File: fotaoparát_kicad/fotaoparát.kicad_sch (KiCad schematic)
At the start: 5 parts, among them IC1 W25Q256JVEIQ, J2 Micro_SD_Card_Det1, U2 CR2013-MI2120

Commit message: blablabla
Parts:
- removed U2: CR2013-MI2120, Display:CR2013-MI2120, symbol Driver_Display:CR2013-MI2120
- added U2: ~, symbol st_lib:ST7796s
- J2: footprint (none) -> Connector_Card:microSD_HC_Hirose_DM3D-SF
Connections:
- net +3.3V: now also R1.1, U2.1 (VCC), U2.7 (RD); no longer R1.2
- net GND: now also U2.2 (GND)
- net at U1.57 (GPIO28): now also U2.23 (D15)
- net at U1.58 (GPIO29): now also U2.22 (D14)
- net at U1.60 (GPIO30): now also U2.21 (D13)
- net at U1.61 (GPIO31): now also U2.19 (D11)
- net at U1.63 (GPIO32): now also U2.18 (D10)
- net at U1.64 (GPIO33): now also U2.17 (D9)
- net at U1.65 (GPIO34): now also U2.16 (D8)
- net at U1.66 (GPIO35): now also U2.15 (D7)
- net at U1.67 (VDD_PSRAM_1): now also U2.14 (D6)
- net at U1.68 (GPIO36): now also U2.13 (D5)
- net at U1.69 (GPIO37): now also U2.12 (D4)
- net at U1.70 (GPIO38): now also U2.11 (D3)
- net at U1.80 (GPIO39): now also U2.10 (D2)
- net at U1.81 (GPIO40): now also U2.9 (D1)
- net at U1.82 (GPIO41): now also U2.8 (D0)
- net at U1.83 (GPIO42): now also U2.6 (WR)
- net at U1.84 (GPIO43): now also U2.5 (RS/DC)
- net at U1.86 (GPIO44): now also U2.4 (CS)
- net at U1.87 (GPIO45): now also U2.3 (RESET)
- net at IC1.3 (DO_(IO1)_2), IC1.7 (IO3): now also R1.2; no longer R1.1
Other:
- moved on the sheet: IC1, J2, R1, U1

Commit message: nevim, neco tu vadi
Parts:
- U2: footprint (none) -> stlib:ST7796s_40PIN_0.8MM
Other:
- moved on the sheet: IC1, J2, R1, U1, U2

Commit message: Mirne nakresove zmeny
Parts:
- added J1: Conn_01x22, Connector_FFC-FPC:Amphenol_F32Q-1A7x1-11022_1x22-1MP_P0.5mm_Horizontal, symbol Connector_Generic:Conn_01x22
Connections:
- net +3.3V: now also J1.1 (Pin_1), J1.2 (Pin_2); no longer U1.85 (VDD_IO_5)
- net GND: now also J1.13 (Pin_13), J1.16 (Pin_16), J1.19 (Pin_19), J1.22 (Pin_22)
- net at U1.42 (CSI_DATAN0): now also J1.21 (Pin_21)
- net at U1.43 (CSI_DATAP0): now also J1.20 (Pin_20)
- net at U1.44 (CSI_CLKP): now also J1.14 (Pin_14)
- net at U1.45 (CSI_CLKN): now also J1.15 (Pin_15)
- net at U1.46 (CSI_DATAN1): now also J1.18 (Pin_18)
- net at U1.47 (CSI_DATAP1): now also J1.17 (Pin_17)
- net at U1.57 (GPIO28): now also J1.3 (Pin_3); no longer U2.23 (D15)
- net at U1.58 (GPIO29): now also J1.4 (Pin_4); no longer U2.22 (D14)
- net at U1.60 (GPIO30): now also J1.6 (Pin_6); no longer U2.21 (D13)
- net at U1.61 (GPIO31): no longer U2.19 (D11)
- net at U1.63 (GPIO32): no longer U2.18 (D10)
- net at U1.64 (GPIO33): no longer U2.17 (D9)
- net at U1.65 (GPIO34): no longer U2.16 (D8)
- net at U1.66 (GPIO35): no longer U2.15 (D7)
- net at U1.67 (VDD_PSRAM_1): no longer U2.14 (D6)
- net at U1.68 (GPIO36): no longer U2.13 (D5)
- net at U1.69 (GPIO37): no longer U2.12 (D4)
- net at U1.70 (GPIO38): no longer U2.11 (D3)
- net at U1.80 (GPIO39): no longer U2.10 (D2)
- net at U1.81 (GPIO40): no longer U2.9 (D1)
- net at U1.82 (GPIO41): no longer U2.8 (D0)
- net at U1.83 (GPIO42): no longer U2.6 (WR)
- net at U1.84 (GPIO43): no longer U2.5 (RS/DC)
- net at U1.86 (GPIO44): no longer U2.4 (CS)
- net at U1.87 (GPIO45): no longer U2.3 (RESET)
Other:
- moved on the sheet: IC1, J2, R1, U1, U2

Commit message: PCB routing 22pin na kameru
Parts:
- J1: footprint Connector_FFC-FPC:Amphenol_F32Q-1A7x1-11022_1x22-1MP_P0.5mm_Horizontal -> rnd_shit_co_nema_symboly:Hirose_FH12-22S-0.5SH
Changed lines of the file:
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@@
 			)
 		)
-		(property "Footprint" "Connector_FFC-FPC:Amphenol_F32Q-1A7x1-11022_1x22-1MP_P0.5mm_Horizontal"
+		(property "Footprint" "rnd_shit_co_nema_symboly:Hirose_FH12-22S-0.5SH"
 			(at 312.42 185.42 0)
 			(effects

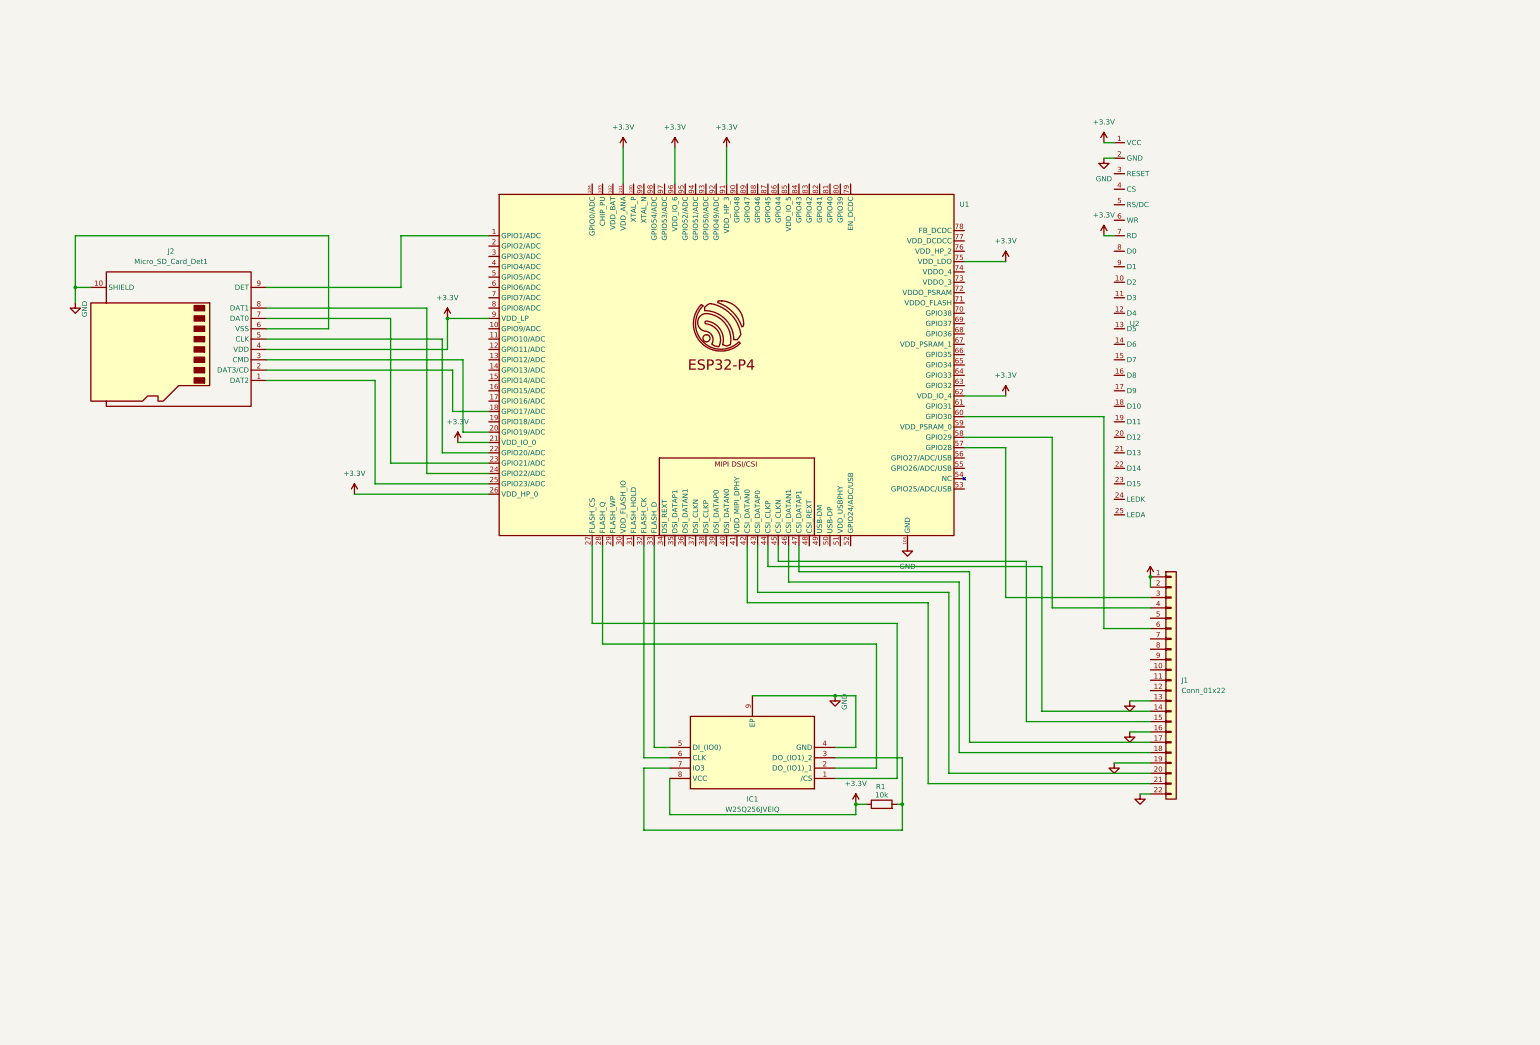
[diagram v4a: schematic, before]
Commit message: Uprava pcb, finalni predelani (snad)  kamery
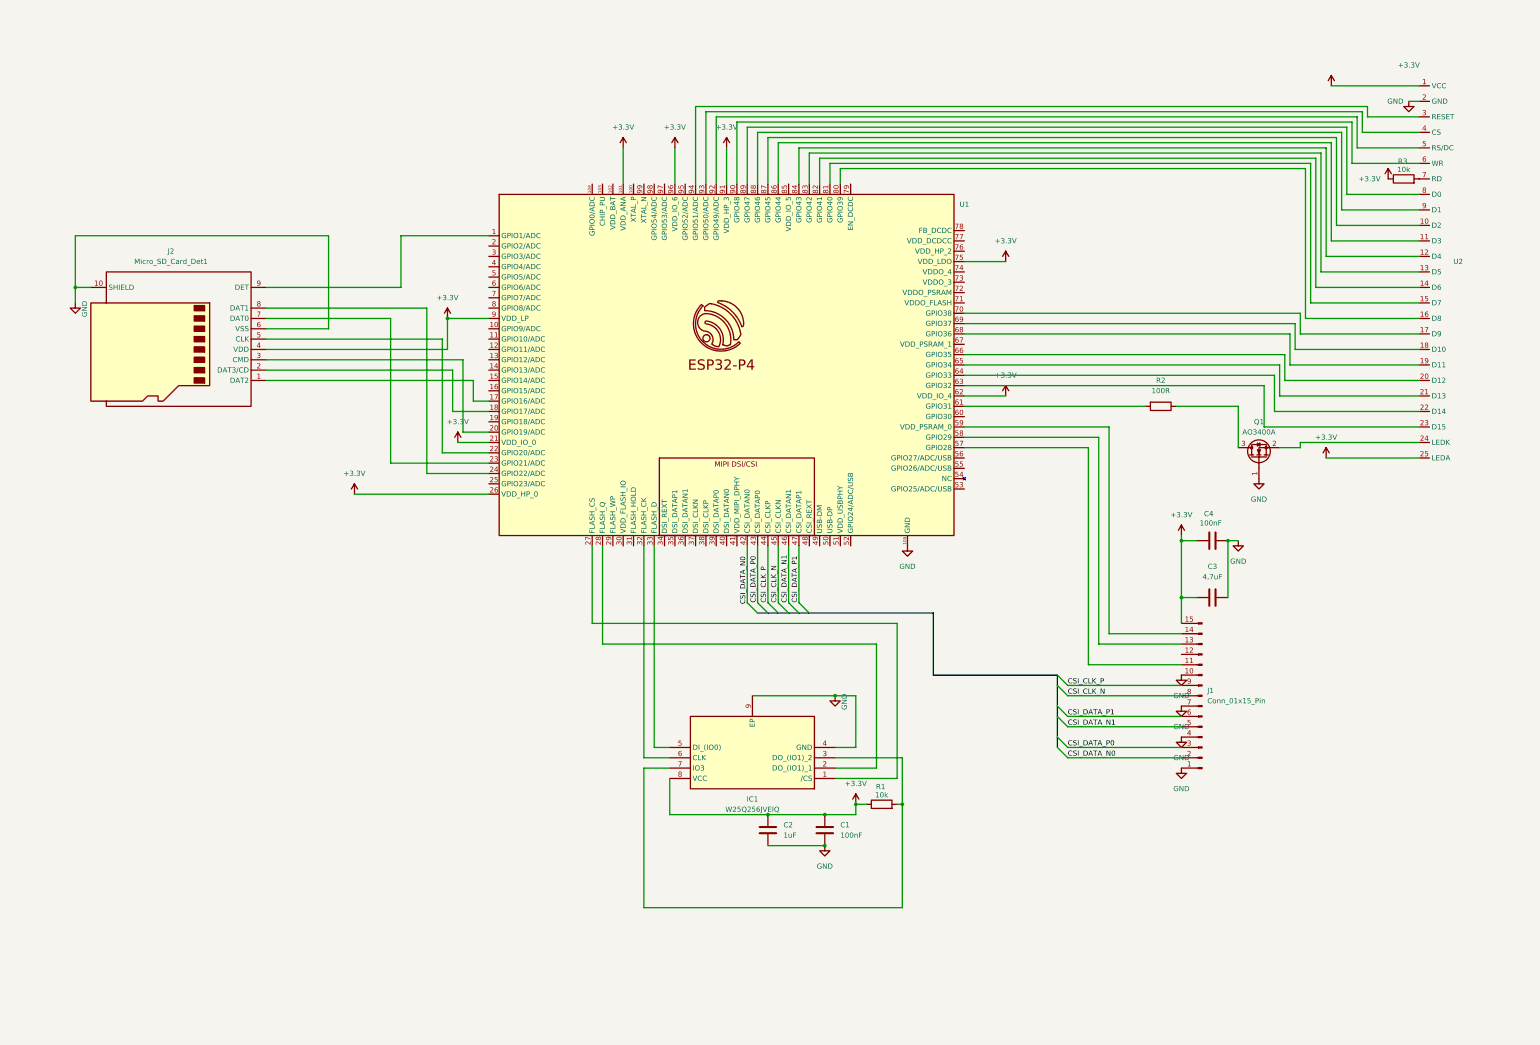
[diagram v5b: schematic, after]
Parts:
- removed J1: Conn_01x22, rnd_shit_co_nema_symboly:Hirose_FH12-22S-0.5SH, symbol Connector_Generic:Conn_01x22
- added C1, C4: 100nF, Capacitor_SMD:C_0201_0603Metric, symbol Device:C
- added C2: 1uF, Capacitor_SMD:C_0201_0603Metric, symbol Device:C
- added C3: 4,7uF, Capacitor_SMD:C_0201_0603Metric, symbol Device:C
- added J1: Conn_01x15_Pin, Connector_FFC-FPC:Hirose_FH12-15S-0.5SH_1x15-1MP_P0.50mm_Horizontal, symbol Connector:Conn_01x15_Pin
- added Q1: AO3400A, Package_TO_SOT_SMD:SOT-23, symbol Transistor_FET:AO3400A
- added R2: 100R, Resistor_SMD:R_0603_1608Metric, symbol Device:R
- added R3: 10k, Resistor_SMD:R_0603_1608Metric, symbol Device:R
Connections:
- net +3.3V: now also U2.25 (LEDA), C1.1, C2.1, C3.1, C4.1, J1.15 (Pin_15), R3.1; no longer U2.7 (RD)
- net GND: now also C1.2, C2.2, C3.2, C4.2, J1.1 (Pin_1), J1.10 (Pin_10), J1.4 (Pin_4), J1.7 (Pin_7), Q1.1 (G)
- net at U1.17 (GPIO16/ADC): now also J2.1 (DAT2)
- net at U1.25 (GPIO23/ADC): no longer J2.1 (DAT2)
- net CSI_DATA_N0: now reaches U1.42 (CSI_DATAN0)
- net CSI_DATA_N0: now also J1.2 (Pin_2)
- net CSI_DATA_P0: now reaches U1.43 (CSI_DATAP0)
- net CSI_DATA_P0: now also J1.3 (Pin_3)
- net CSI_CLK_P: now reaches U1.44 (CSI_CLKP)
- net CSI_CLK_P: now also J1.9 (Pin_9)
- net CSI_CLK_N: now reaches U1.45 (CSI_CLKN)
- net CSI_CLK_N: now also J1.8 (Pin_8)
- net CSI_DATA_N1: now reaches U1.46 (CSI_DATAN1)
- net CSI_DATA_N1: now also J1.5 (Pin_5)
- net CSI_DATA_P1: now reaches U1.47 (CSI_DATAP1)
- net CSI_DATA_P1: now also J1.6 (Pin_6)
- net at U1.57 (GPIO28): now also J1.11 (Pin_11)
- net at U1.58 (GPIO29): now also J1.13 (Pin_13)
- net at U1.59 (VDD_PSRAM_0): now also J1.14 (Pin_14)
- net at U1.61 (GPIO31): now also R2.2
- net at U1.63 (GPIO32): now also U2.23 (D15)
- net at U1.64 (GPIO33): now also U2.22 (D14)
- net at U1.65 (GPIO34): now also U2.21 (D13)
- net at U1.66 (GPIO35): now also U2.20 (D12)
- net at U1.68 (GPIO36): now also U2.19 (D11)
- net at U1.69 (GPIO37): now also U2.18 (D10)
- net at U1.70 (GPIO38): now also U2.17 (D9)
- net at U1.80 (GPIO39): now also U2.16 (D8)
- net at U1.81 (GPIO40): now also U2.15 (D7)
- net at U1.82 (GPIO41): now also U2.14 (D6)
- net at U1.83 (GPIO42): now also U2.13 (D5)
- net at U1.84 (GPIO43): now also U2.12 (D4)
- net at U1.86 (GPIO44): now also U2.11 (D3)
- net at U1.87 (GPIO45): now also U2.10 (D2)
- net at U1.88 (GPIO46): now also U2.9 (D1)
- net at U1.89 (GPIO47): now also U2.8 (D0)
- net at U1.90 (GPIO48): now also U2.6 (WR)
- net at U1.92 (GPIO49/ADC): now also U2.5 (RS/DC)
- net at U1.93 (GPIO50/ADC): now also U2.4 (CS)
- net at U1.94 (GPIO51/ADC): now also U2.3 (RESET)
- net at U2.24 (LEDK): now also Q1.2 (S)
- new net: R3.2, U2.7 (RD)
- new net: Q1.3 (D), R2.1
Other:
- moved on the sheet: U2

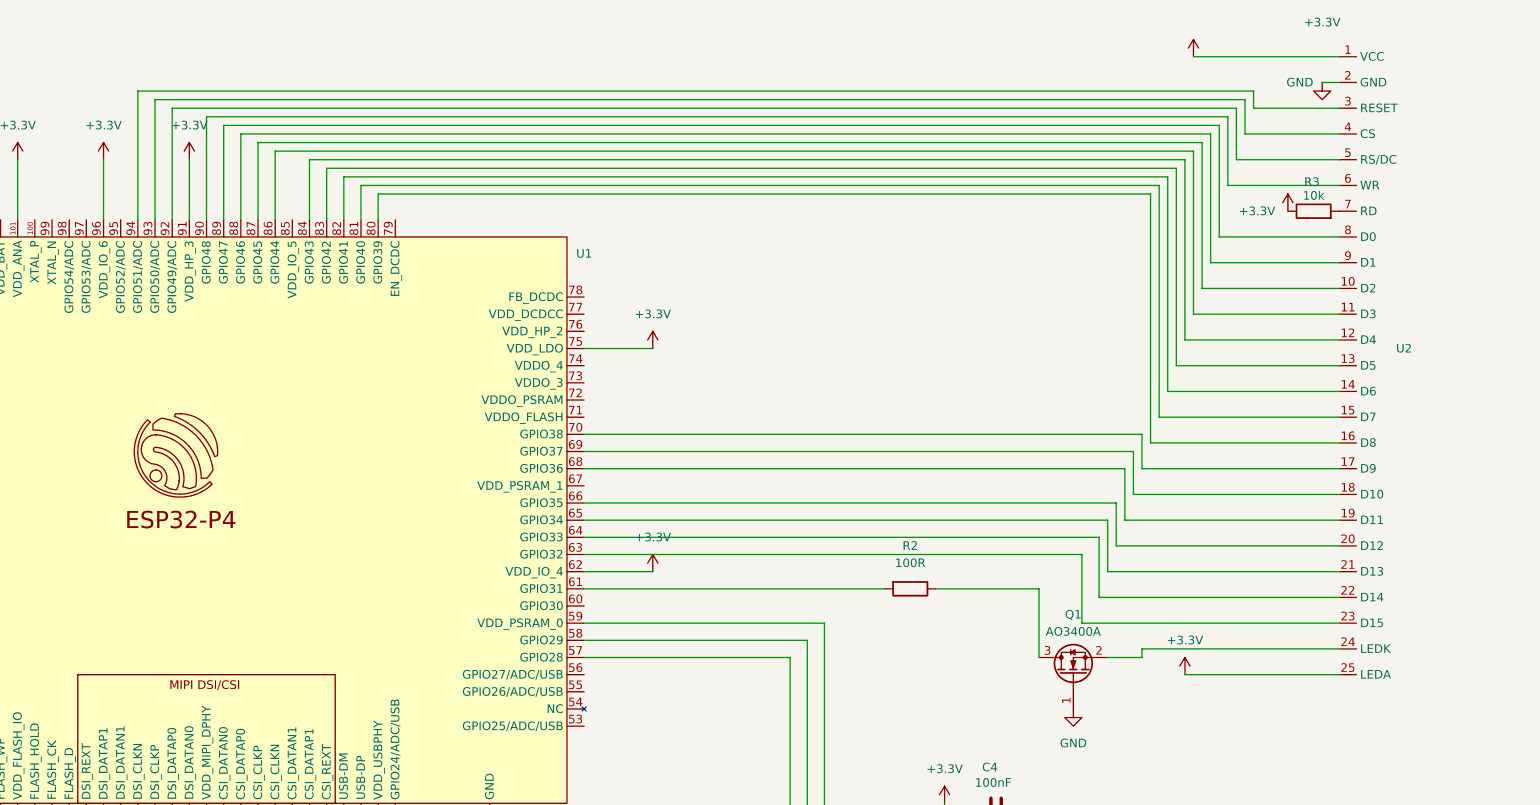
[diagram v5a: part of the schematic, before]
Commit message: Zvyseni prehlednosti schametu
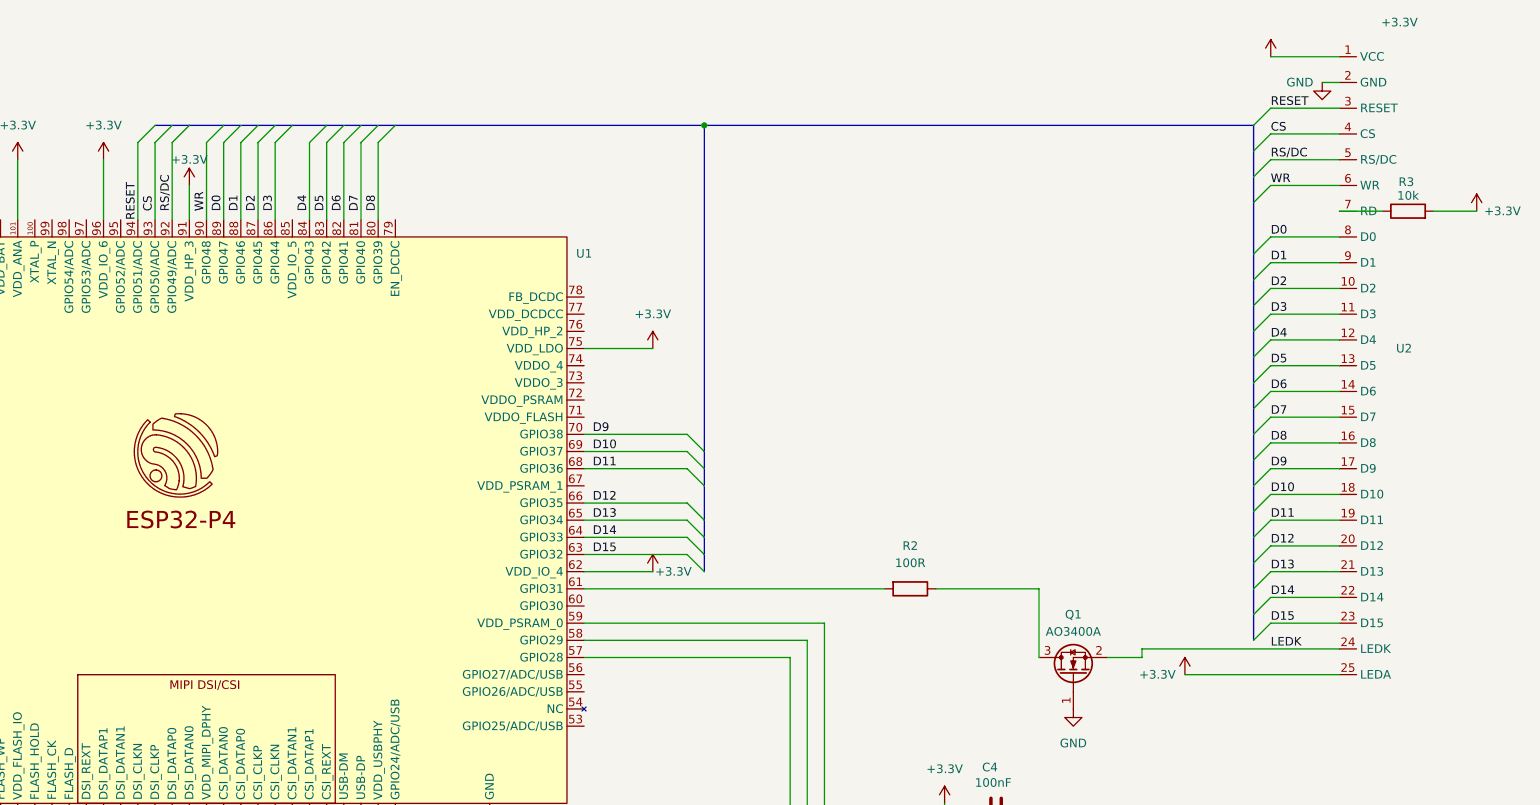
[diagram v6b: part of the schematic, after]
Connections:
- net +3.3V: now also R3.2; no longer R3.1
- net D15: now reaches U1.63 (GPIO32), U2.23 (D15)
- net D14: now reaches U1.64 (GPIO33), U2.22 (D14)
- net D13: now reaches U1.65 (GPIO34), U2.21 (D13)
- net D12: now reaches U1.66 (GPIO35), U2.20 (D12)
- net D11: now reaches U1.68 (GPIO36), U2.19 (D11)
- net D10: now reaches U1.69 (GPIO37), U2.18 (D10)
- net D9: now reaches U1.70 (GPIO38), U2.17 (D9)
- net D8: now reaches U1.80 (GPIO39), U2.16 (D8)
- net D7: now reaches U1.81 (GPIO40), U2.15 (D7)
- net D6: now reaches U1.82 (GPIO41), U2.14 (D6)
- net D5: now reaches U1.83 (GPIO42), U2.13 (D5)
- net D4: now reaches U1.84 (GPIO43), U2.12 (D4)
- net D3: now reaches U1.86 (GPIO44), U2.11 (D3)
- net D2: now reaches U1.87 (GPIO45), U2.10 (D2)
- net D1: now reaches U1.88 (GPIO46), U2.9 (D1)
- net D0: now reaches U1.89 (GPIO47), U2.8 (D0)
- net WR: now reaches U1.90 (GPIO48), U2.6 (WR)
- net RS/DC: now reaches U1.92 (GPIO49/ADC), U2.5 (RS/DC)
- net CS: now reaches U1.93 (GPIO50/ADC), U2.4 (CS)
- net RESET: now reaches U1.94 (GPIO51/ADC), U2.3 (RESET)
- net at U2.7 (RD): now also R3.1; no longer R3.2
- net LEDK: now reaches Q1.2 (S), U2.24 (LEDK)
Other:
- moved on the sheet: R3
